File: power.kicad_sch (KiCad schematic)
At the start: 18 parts, among them J1 USB_C_Receptacle_USB2.0_14P, J8 Conn_01x04, J9 Conn_01x04, U4 TPS6282x

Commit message: schem: update +5v tvs diode part #
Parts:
- removed D7, D8: H5VU10U, GLCS:Diode_DFN1006, symbol GLCS:H5VU10U
- added D7, D8: SMBJ6.0CA, Diode_SMD:D_SMB, symbol Device:D_TVS
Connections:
- net Efuse/+VIN: now also D7.1 (A1), D8.1 (A1)
- net GND: now also D7.2 (A2), D8.2 (A2)

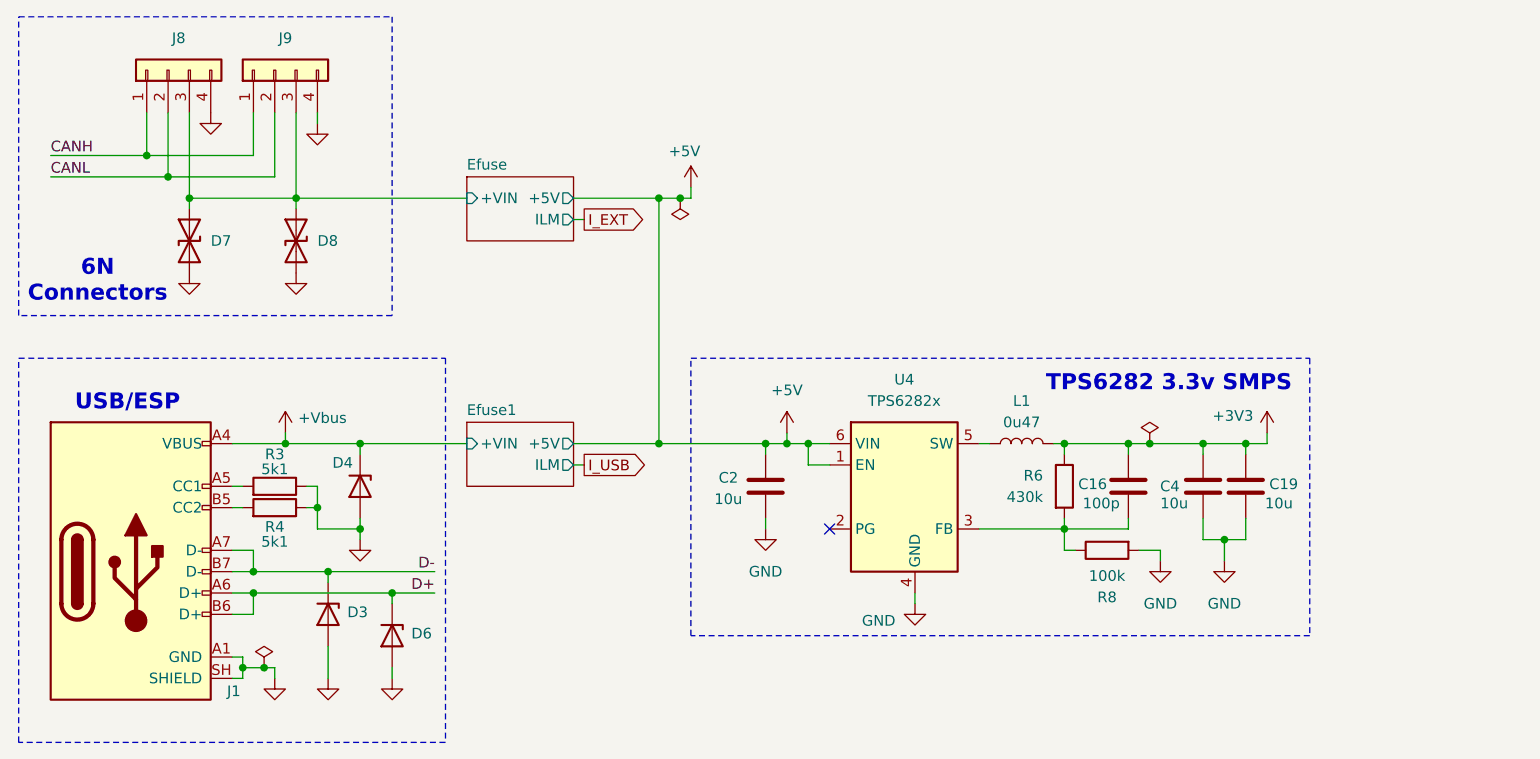
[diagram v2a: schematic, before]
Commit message: schem: add test points
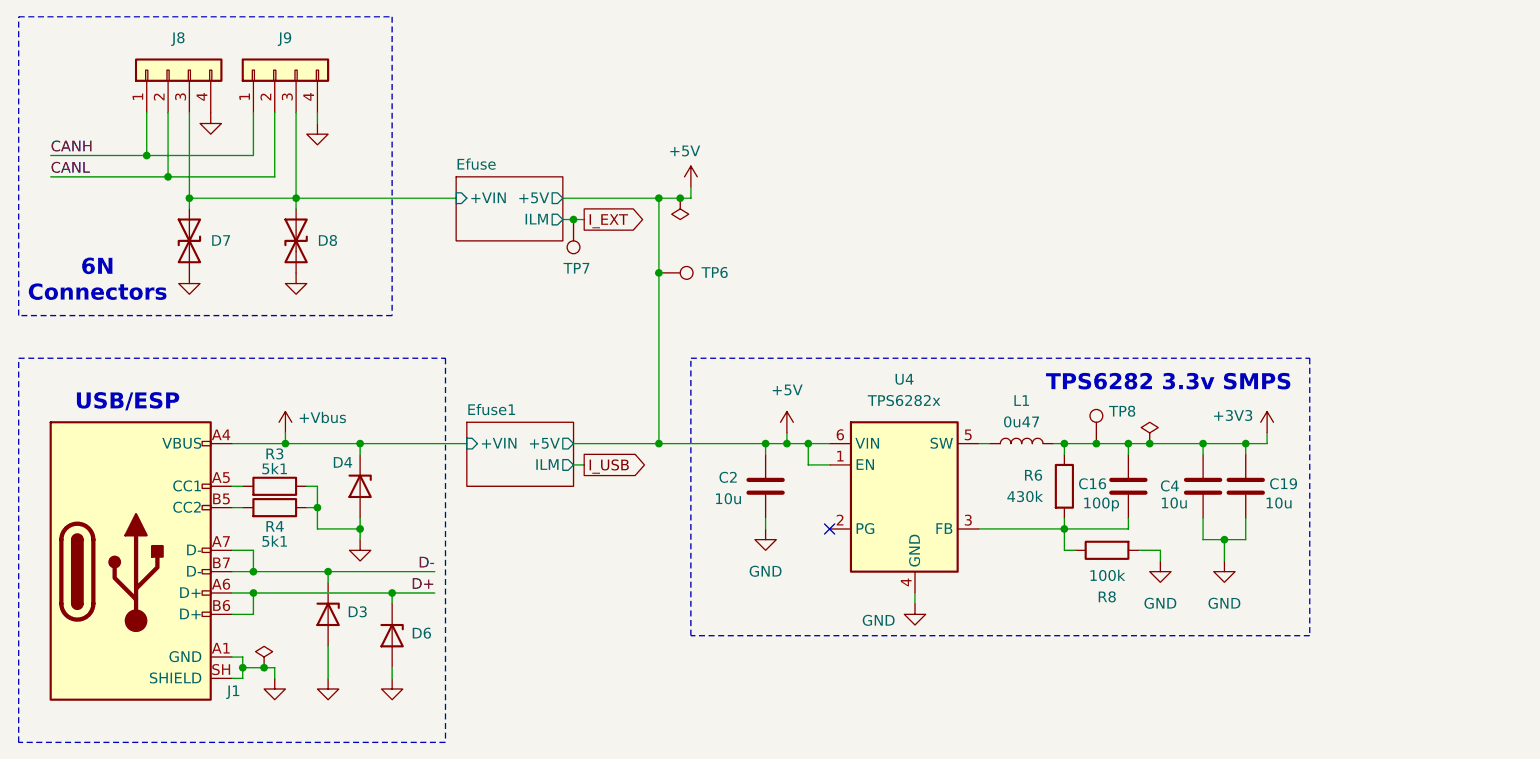
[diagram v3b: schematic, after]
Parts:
- added TP6, TP7, TP8: TestPoint, TestPoint:TestPoint_Pad_D2.0mm, symbol Connector:TestPoint
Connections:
- net +3V3: now also TP8.1
- net +5V: now also TP6.1
- net I_EXT: now also TP7.1

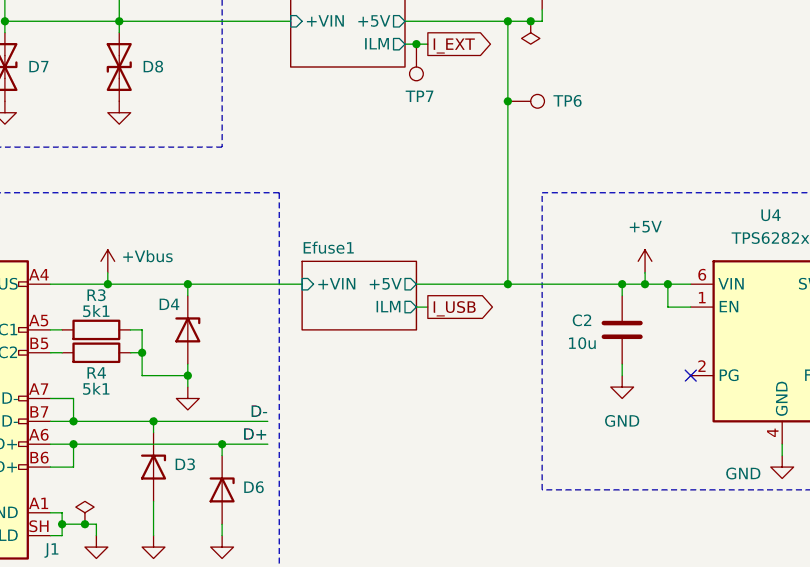
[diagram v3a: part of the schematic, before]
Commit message: schem: replace vbus efuse with diode
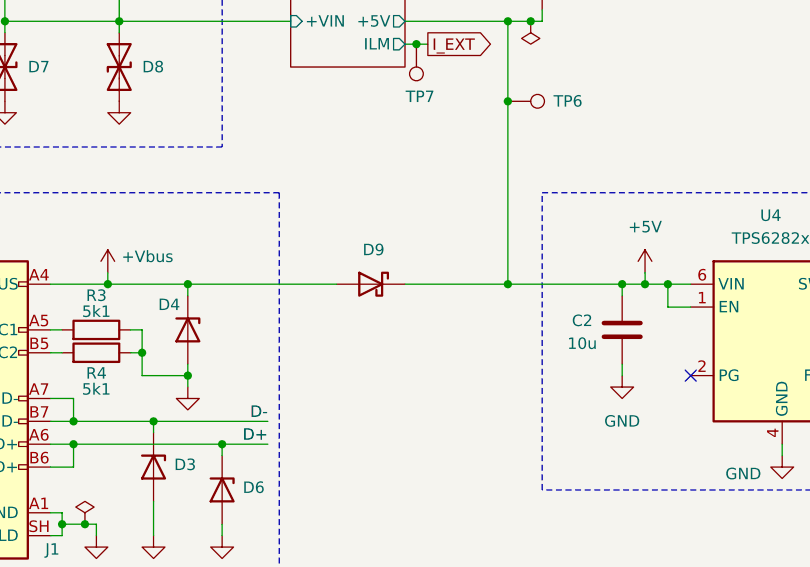
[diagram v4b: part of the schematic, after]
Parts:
- added D9: D_Schottky, Diode_SMD:D_SMA, symbol Device:D_Schottky
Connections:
- net +5V: now also D9.1 (K)
- net +Vbus: now also D9.2 (A)
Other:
- removed sheet Efuse1
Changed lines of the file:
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@@
 	)
 	(junction
-		(at 147.32 107.95)
-		(diameter 0)
-		(color 0 0 0 0)
-	)
-	(junction
 		(at 147.32 78.74)
 		(diameter 0)
@@
 	)
 	(junction
-		(at 111.76 107.95)
-		(diameter 0)
-		(color 0 0 0 0)
-	)
-	(junction
 		(at 99.06 123.19)
 		(diameter 0)
@@
 	)
 	(junction
-		(at 99.06 125.73)
+		(at 111.76 107.95)
 		(diameter 0)
 		(color 0 0 0 0)
 	)
 	(junction
-		(at 162.56 107.95)
+		(at 99.06 125.73)
 		(diameter 0)
 		(color 0 0 0 0)
 	)
 	(junction
-		(at 160.02 107.95)
+		(at 162.56 107.95)
 		(diameter 0)
 		(color 0 0 0 0)
@@
 	)
 	(junction
+		(at 147.32 107.95)
+		(diameter 0)
+		(color 0 0 0 0)
+	)
+	(junction
 		(at 111.76 118.11)
 		(diameter 0)
@@
 		(color 0 0 0 0)
 	)
+	(junction
+		(at 160.02 107.95)
+		(diameter 0)
+		(color 0 0 0 0)
+	)
 	(no_connect
 		(at 167.64 118.11)
@@
 	(wire
 		(pts
-			(xy 111.76 107.95) (xy 124.46 107.95)
-		)
-		(stroke
-			(width 0)
-			(type default)
-		)
-	)
-	(wire
-		(pts
 			(xy 115.57 135.89) (xy 115.57 134.62)
 		)
@@
 	(wire
 		(pts
-			(xy 137.16 107.95) (xy 160.02 107.95)
-		)
-		(stroke
-			(width 0)
-			(type default)
-		)
-	)
-	(wire
-		(pts
 			(xy 101.6 68.58) (xy 101.6 76.2)
 		)
@@
 	(wire
 		(pts
-			(xy 138.43 110.49) (xy 137.16 110.49)
-		)
-		(stroke
-			(width 0)
-			(type default)
-		)
-	)
-	(wire
-		(pts
 			(xy 111.76 119.38) (xy 111.76 118.11)
 		)
@@
 	(wire
 		(pts
+			(xy 111.76 107.95) (xy 128.27 107.95)
+		)
+		(stroke
+			(width 0)
+			(type default)
+		)
+	)
+	(wire
+		(pts
 			(xy 106.68 115.57) (xy 105.41 115.57)
 		)
@@
 	(wire
 		(pts
+			(xy 147.32 107.95) (xy 160.02 107.95)
+		)
+		(stroke
+			(width 0)
+			(type default)
+		)
+	)
+	(wire
+		(pts
 			(xy 212.09 107.95) (xy 217.17 107.95)
 		)
@@
 	(wire
 		(pts
+			(xy 135.89 107.95) (xy 147.32 107.95)
+		)
+		(stroke
+			(width 0)
+			(type default)
+		)
+	)
+	(wire
+		(pts
 			(xy 214.63 119.38) (xy 214.63 121.92)
 		)
@@
 		)
 	)
-	(global_label "I_USB"
-		(shape output)
-		(at 138.43 110.49 0)
-		(effects
-			(font
-				(size 1.27 1.27)
-			)
-			(justify left)
-		)
-		(property "Intersheetrefs" "${INTERSHEET_REFS}"
-			(at 138.43 110.49 0)
-			(hide yes)
-			(show_name no)
-			(do_not_autoplace no)
-			(effects
-				(font
-					(size 1.27 1.27)
-				)
-			)
-		)
-	)
 	(global_label "I_EXT"
 		(shape output)
@@
 	)
 	(symbol
+		(lib_id "Device:D_Schottky")
+		(at 132.08 107.95 0)
+		(mirror y)
+		(unit 1)
+		(body_style 1)
+		(exclude_from_sim no)
+		(in_bom yes)
+		(on_board yes)
+		(in_pos_files yes)
+		(dnp no)
+		(fields_autoplaced yes)
+		(property "Reference" "D9"
+			(at 132.3975 104.14 0)
+			(show_name no)
+			(do_not_autoplace no)
+			(effects
+				(font
+					(size 1.27 1.27)
+				)
+			)
+		)
+		(property "Value" "D_Schottky"
+			(at 132.3975 104.14 0)
+			(hide yes)
+			(show_name no)
+			(do_not_autoplace no)
+			(effects
+				(font
+					(size 1.27 1.27)
+				)
+			)
+		)
+		(property "Footprint" "Diode_SMD:D_SMA"
+			(at 132.08 107.95 0)
+			(hide yes)
+			(show_name no)
+			(do_not_autoplace no)
+			(effects
+				(font
+					(size 1.27 1.27)
+				)
+			)
+		)
+		(property "Datasheet" ""
+			(at 132.08 107.95 0)
+			(hide yes)
+			(show_name no)
+			(do_not_autoplace no)
+			(effects
+				(font
+					(size 1.27 1.27)
+				)
+			)
+		)
+		(property "Description" "Schottky diode"
+			(at 132.08 107.95 0)
+			(hide yes)
+			(show_name no)
+			(do_not_autoplace no)
+			(effects
+				(font
+					(size 1.27 1.27)
+				)
+			)
+		)
+		(property "Manufacturer" "Microdiode Semiconductor (MDD)"
+			(at 132.08 107.95 0)
+			(hide yes)
+			(show_name no)
+			(do_not_autoplace no)
+			(effects
+				(font
+					(size 1.27 1.27)
+				)
+			)
+		)
+		(property "Manufacturer Part Number" "SS54"
+			(at 132.08 107.95 0)
+			(hide yes)
+			(show_name no)
+			(do_not_autoplace no)
+			(effects
+				(font
+					(size 1.27 1.27)
+				)
+			)
+		)
+		(property "Basic" "Y"
+			(at 132.08 107.95 0)
+			(hide yes)
+			(show_name no)
+			(do_not_autoplace no)
+			(effects
+				(font
+					(size 1.27 1.27)
+				)
+			)
+		)
+		(property "JLCPCB Part #" "C22452"
+			(at 132.08 107.95 0)
+			(hide yes)
+			(show_name no)
+			(do_not_autoplace no)
+			(effects
+				(font
+					(size 1.27 1.27)
+				)
+			)
+		)
+		(pin "2"
+		)
+		(pin "1"
+		)
+		(instances
+			(project "s6tm-detect-cb-2"
+				(path "/f4a18219-a653-4da9-9eb6-662d05c28432/169cf3bf-dcdd-445b-abbd-86da239eca7a"
+					(reference "D9")
+					(unit 1)
+				)
+			)
+		)
+	)
+	(symbol
 		(lib_id "GLCS:H5VU10U")
 		(at 107.95 128.27 270)
@@
 				)
 			)
-		)
-	)
-	(sheet
-		(at 124.46 105.41)
-		(size 12.7 7.62)
-		(exclude_from_sim no)
-		(in_bom yes)
-		(on_board yes)
-		(dnp no)
-		(fields_autoplaced yes)
-		(stroke
-			(width 0.1524)
-			(type solid)
-		)
-		(fill
-			(color 0 0 0 0)
-		)
-		(property "Sheetname" "Efuse1"
-			(at 124.46 104.6984 0)
-			(show_name no)
-			(do_not_autoplace no)
-			(effects
-				(font
-					(size 1.27 1.27)
-				)
-				(justify left bottom)
-			)
-		)
-		(property "Sheetfile" "efuse.kicad_sch"
-			(at 124.46 113.6146 0)
-			(hide yes)
-			(show_name no)
-			(do_not_autoplace no)
-			(effects
-				(font
-					(size 1.27 1.27)
-				)
-				(justify left top)
-			)
-		)
-		(pin "+5V" output
-			(at 137.16 107.95 0)
-			(effects
-				(font
-					(size 1.27 1.27)
-				)
-				(justify right)
-			)
-		)
-		(pin "+VIN" input
-			(at 124.46 107.95 180)
-			(effects
-				(font
-					(size 1.27 1.27)
-				)
-				(justify left)
-			)
-		)
-		(pin "ILM" output
-			(at 137.16 110.49 0)
-			(effects
-				(font
-					(size 1.27 1.27)
-				)
-				(justify right)
-			)
-		)
-		(instances
-			(project "s6tm-detect-cb-2"
-				(path "/f4a18219-a653-4da9-9eb6-662d05c28432/169cf3bf-dcdd-445b-abbd-86da239eca7a"
-					(page "4")
-				)
-			)

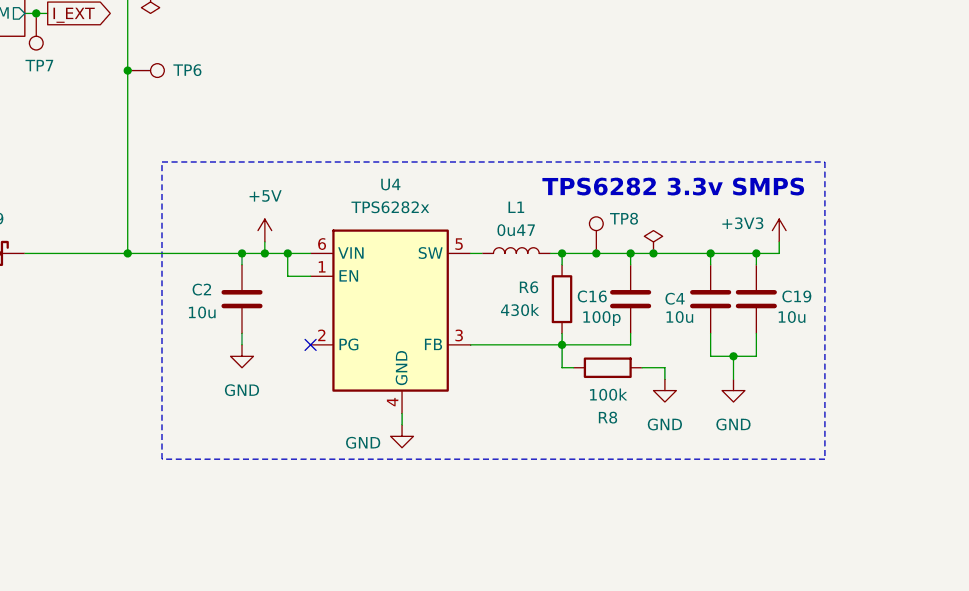
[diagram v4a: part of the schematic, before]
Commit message: schem: add +3v3 bulk decoupling caps
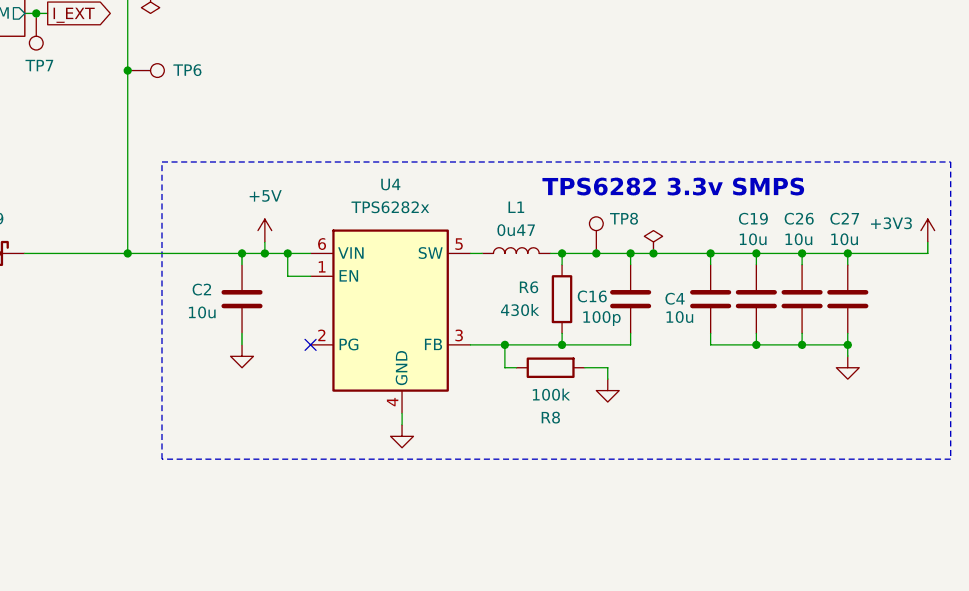
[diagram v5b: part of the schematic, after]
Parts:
- added C26, C27: 10u, Capacitor_SMD:C_0402_1005Metric, symbol Device:C
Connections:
- net +3V3: now also C26.1, C27.1
- net GND: now also C26.2, C27.2
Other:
- moved on the sheet: R8

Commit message: schem: add +3v8 smps
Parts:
- added C28: 10u, Capacitor_SMD:C_0603_1608Metric, symbol Device:C
- added C29: 100p, Capacitor_SMD:C_0402_1005Metric, symbol Device:C
- added C36, C37, C38, C39: 10u, Capacitor_SMD:C_0402_1005Metric, symbol Device:C
- added L2: 0u47, Pers:TDK_TFM201610ALC, symbol Device:L
- added R14: 100k, Resistor_SMD:R_0402_1005Metric, symbol Device:R
- added R15: 560k, Resistor_SMD:R_0603_1608Metric, symbol Device:R
- added R16: 510, Resistor_SMD:R_0603_1608Metric, symbol Device:R
- added TP9: TestPoint, TestPoint:TestPoint_Pad_D2.0mm, symbol Connector:TestPoint
- added U10: TPS6282x, Pers:Texas_VSON-6_1.5x1.5mm_P0.5mm_DMQ0006A, symbol Pers:TPS6282x
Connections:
- net +5V: now also C28.1, U10.1 (EN), U10.6 (VIN)
- net GND: now also C28.2, C36.2, C37.2, C38.2, C39.2, R14.2, U10.4 (GND)
- new net: C29.2, R14.1, R15.2, R16.2, U10.3 (FB)
- new net: L2.1, U10.5 (SW)
- new net +3V8: C29.1, C36.1, C37.1, C38.1, C39.1, L2.2, R15.1, R16.1, TP9.1
- no-connect marks 1 -> 2
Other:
- note added: "TPS6282 3.8v SMPS"
- moved on the sheet: C16, C19, C2, C26, C27, C4, L1, R6, R8, TP8, U4

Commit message: schem: run and fix ERC
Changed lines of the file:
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@@
 	(rectangle
 		(start 71.12 97.79)
-		(end 121.92 143.51)
+		(end 124.46 143.51)
 		(stroke
 			(width 0)
@@
 	)
 	(junction
-		(at 149.86 78.74)
-		(diameter 0)
-		(color 0 0 0 0)
-	)
-	(junction
 		(at 173.99 71.12)
 		(diameter 0)
@@
 	(wire
 		(pts
-			(xy 115.57 125.73) (xy 120.65 125.73)
+			(xy 115.57 125.73) (xy 116.84 125.73)
 		)
 		(stroke
@@
 	(wire
 		(pts
-			(xy 99.06 123.19) (xy 120.65 123.19)
+			(xy 99.06 123.19) (xy 116.84 123.19)
 		)
 		(stroke
@@
 		)
 	)
-	(label "D-"
-		(at 120.65 123.19 180)
+	(label "CANH"
+		(at 74.93 73.66 0)
 		(effects
 			(font
 				(size 1.27 1.27)
 			)
-			(justify right bottom)
+			(justify left bottom)
 		)
 	)
-	(label "CANH"
-		(at 74.93 73.66 0)
+	(global_label "D+"
+		(shape input)
+		(at 116.84 125.73 0)
+		(fields_autoplaced yes)
 		(effects
 			(font
 				(size 1.27 1.27)
 			)
-			(justify left bottom)
+			(justify left)
+		)
+		(property "Intersheetrefs" "${INTERSHEET_REFS}"
+			(at 122.6676 125.73 0)
+			(hide yes)
+			(show_name no)
+			(do_not_autoplace no)
+			(effects
+				(font
+					(size 1.27 1.27)
+				)
+				(justify left)
+			)
 		)
 	)
-	(label "D+"
-		(at 120.65 125.73 180)
+	(global_label "D-"
+		(shape input)
+		(at 116.84 123.19 0)
+		(fields_autoplaced yes)
 		(effects
 			(font
 				(size 1.27 1.27)
 			)
-			(justify right bottom)
+			(justify left)
+		)
+		(property "Intersheetrefs" "${INTERSHEET_REFS}"
+			(at 122.6676 123.19 0)
+			(hide yes)
+			(show_name no)
+			(do_not_autoplace no)
+			(effects
+				(font
+					(size 1.27 1.27)
+				)
+				(justify left)
+			)
 		)
 	)
@@
 					(unit 1)
 				)
-			)
-		)
-	)
-	(symbol
-		(lib_id "power:PWR_FLAG")
-		(at 149.86 78.74 180)
-		(unit 1)
-		(body_style 1)
-		(exclude_from_sim no)
-		(in_bom yes)
-		(on_board yes)
-		(in_pos_files yes)
-		(dnp no)
-		(fields_autoplaced yes)
-		(property "Reference" "#FLG02"
-			(at 149.86 80.645 0)
-			(hide yes)
-			(show_name no)
-			(do_not_autoplace no)
-			(effects
-				(font
-					(size 1.27 1.27)
-				)
-			)
-		)
-		(property "Value" "PWR_FLAG"
-			(at 149.86 83.82 0)
-			(hide yes)
-			(show_name no)
-			(do_not_autoplace no)
-			(effects
-				(font
-					(size 1.27 1.27)
-				)
-			)
-		)
-		(property "Footprint" ""
-			(at 149.86 78.74 0)
-			(hide yes)
-			(show_name no)
-			(do_not_autoplace no)
-			(effects
-				(font
-					(size 1.27 1.27)
-				)
-			)
-		)
-		(property "Datasheet" ""
-			(at 149.86 78.74 0)
-			(hide yes)
-			(show_name no)
-			(do_not_autoplace no)
-			(effects
-				(font
-					(size 1.27 1.27)
-				)
-			)
-		)
-		(property "Description" "Special symbol for telling ERC where power comes from"
-			(at 149.86 78.74 0)
-			(hide yes)
-			(show_name no)
-			(do_not_autoplace no)
-			(effects
-				(font
-					(size 1.27 1.27)
-				)
-			)
-		)
-		(pin "1"
-		)
-		(instances
-			(project "s6tm-detect-cb-2"
-				(path "/f4a18219-a653-4da9-9eb6-662d05c28432/169cf3bf-dcdd-445b-abbd-86da239eca7a"
-					(reference "#FLG02")
-					(unit 1)
-				)

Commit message: schem: add sheet titles
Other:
- company: (none) -> Rémi Ait-Younes
- title: (none) -> S6TM Detect Carrier 2
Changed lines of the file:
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@@
 	(generator_version "10.0")
 	(paper "A4")
+	(title_block
+		(title "S6TM Detect Carrier 2")
+		(date "2026-09-24")
+		(rev "01")
+		(company "Rémi Ait-Younes")
+	)
 	(rectangle
 		(start 71.12 97.79)
